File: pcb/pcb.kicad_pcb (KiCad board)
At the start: 2 copper layers, 123.2 x 95.9 mm, 31 parts, among them SW1 SW_Push, SW10 SW_Push, SW11 SW_Push, SW12 SW_Push, SW13 SW_Push, SW14 SW_Push, SW15 SW_Push, SW16 SW_Push, SW17 SW_Push, SW18 SW_Push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

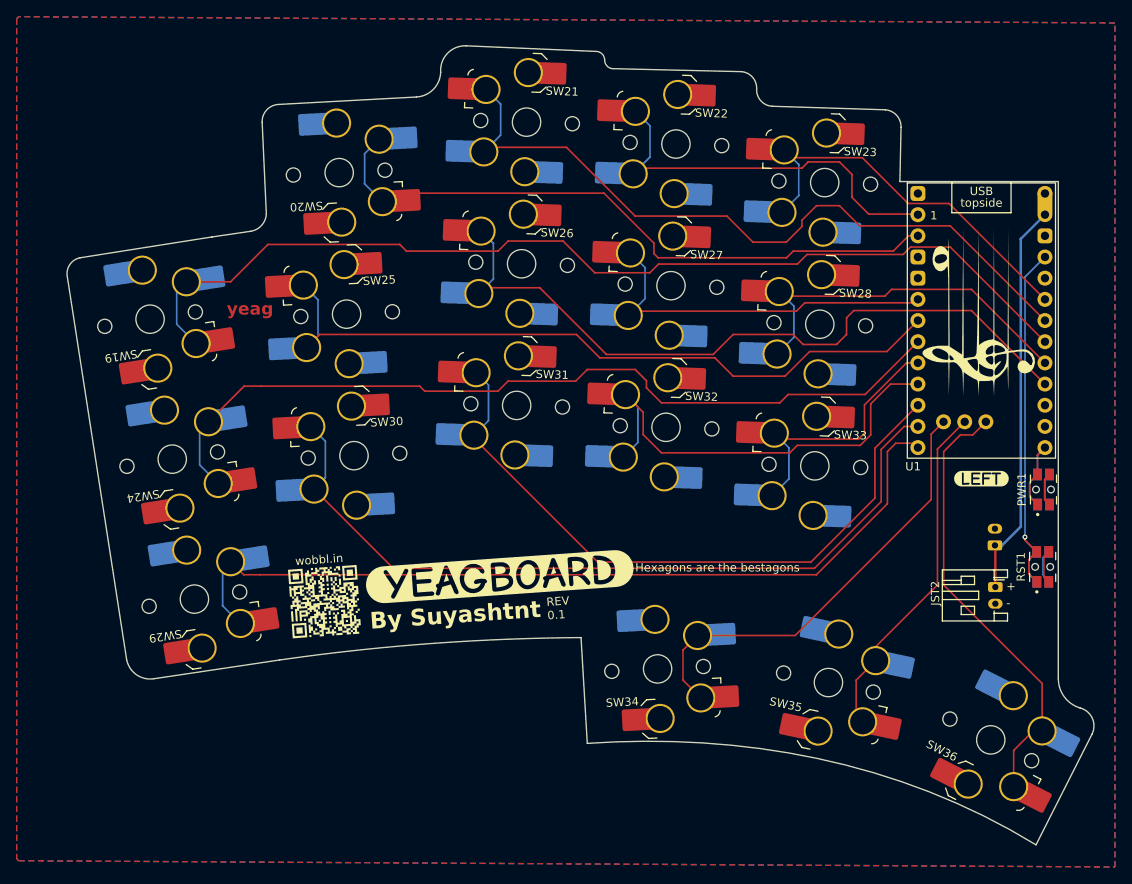
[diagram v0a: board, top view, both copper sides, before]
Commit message: feat: new hotswap footprint + routing
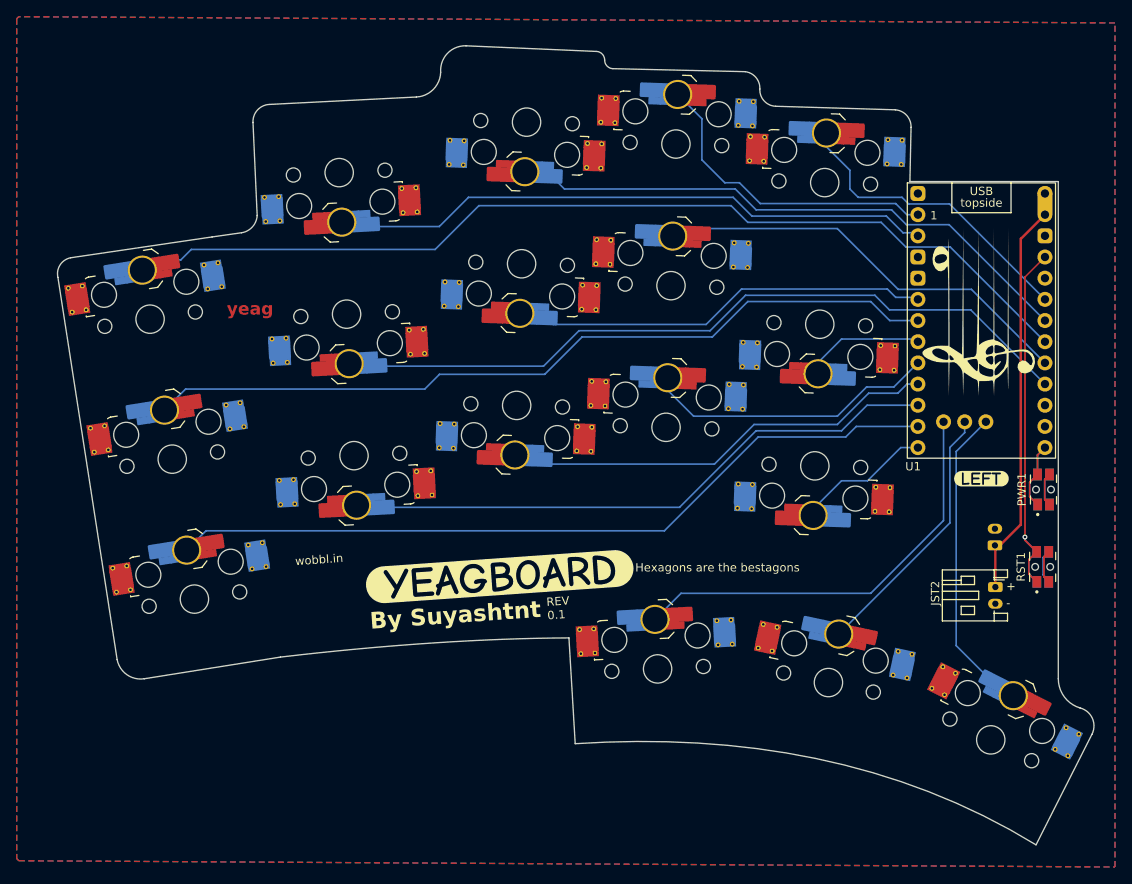
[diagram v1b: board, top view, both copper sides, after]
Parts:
- removed QR*****: WobblQR, Library:WobblQR
- turned SW14 to -2 degrees
- turned SW2 to -177 degrees
- turned SW4 to -2 degrees
- turned SW5 to -2 degrees
- turned SW9 to -2 degrees
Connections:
- U1 pad 10: Switch13 -> Switch12
- U1 pad 11: Switch12 -> Switch11
- U1 pad 12: Switch11 -> Switch15
- U1 pad 20: Switch10 -> Switch9
- U1 pad 21: Switch8 -> Switch7
- U1 pad 5: Switch9 -> Switch8
- U1 pad 6: Switch7 -> Switch6
- U1 pad 7: Switch6 -> Switch10
- U1 pad 8: Switch15 -> Switch14
- U1 pad 9: Switch14 -> Switch13
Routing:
- net Switch8: track 88.3 -> 47.1 mm
- net Switch13: track 79.9 -> 49.3 mm
- net Switch10: track 45.1 -> 14.6 mm
- net Switch12: track 95.9 -> 69.2 mm
- net Switch3: track 89.3 -> 66.4 mm
- net Switch18: track 53.7 -> 34.2 mm
- net Switch14: track 54.0 -> 35.4 mm
- net Switch15: track 32.4 -> 16.4 mm
- net Switch5: track 47.8 -> 36.8 mm
- net Switch4: track 48.0 -> 37.7 mm
- net Switch17: track 41.7 -> 31.7 mm
- net Switch11: track 102.2 -> 93.9 mm
- net Switch9: track 44.6 -> 51.7 mm
- net Switch2: track 75.5 -> 69.3 mm
- net Switch6: track 102.2 -> 96.7 mm
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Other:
- board size 123.2 x 95.9 mm -> 124.3 x 95.9 mm

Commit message: fix: readd QR code
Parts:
- added QR*****: WobblQR, Library:WobblQR, F.Cu at (56.2, 122.8)
